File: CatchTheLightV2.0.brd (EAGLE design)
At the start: 45 x 100 mm, 46 parts, among them J1 TC2030-IDC-NL, U1 ATMEGA328PB-ANR

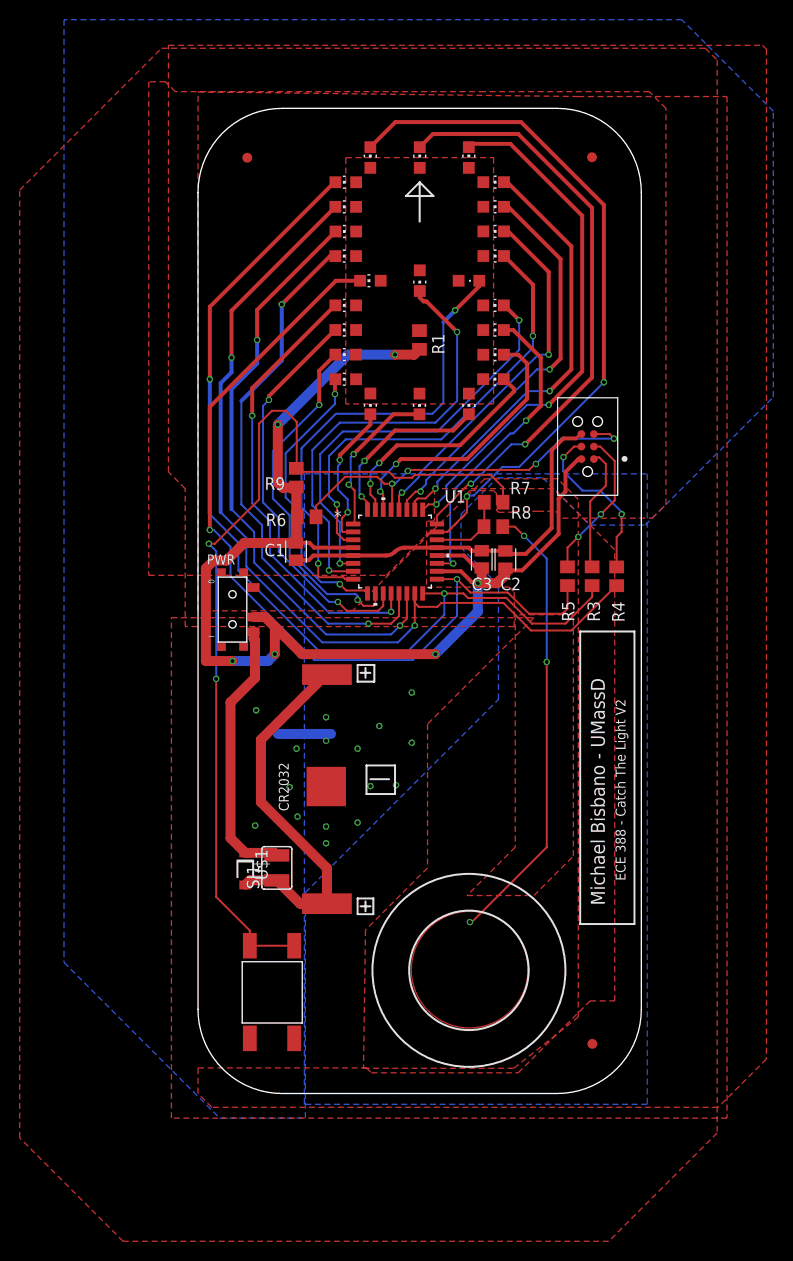
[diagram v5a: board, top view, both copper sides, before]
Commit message: Board Updated to meet some issue requirements
Fiducials relocated according to spec
Silkscreen labels updated

Silkscreen over battery pads removed. Thermal Relief restored on GND pad.
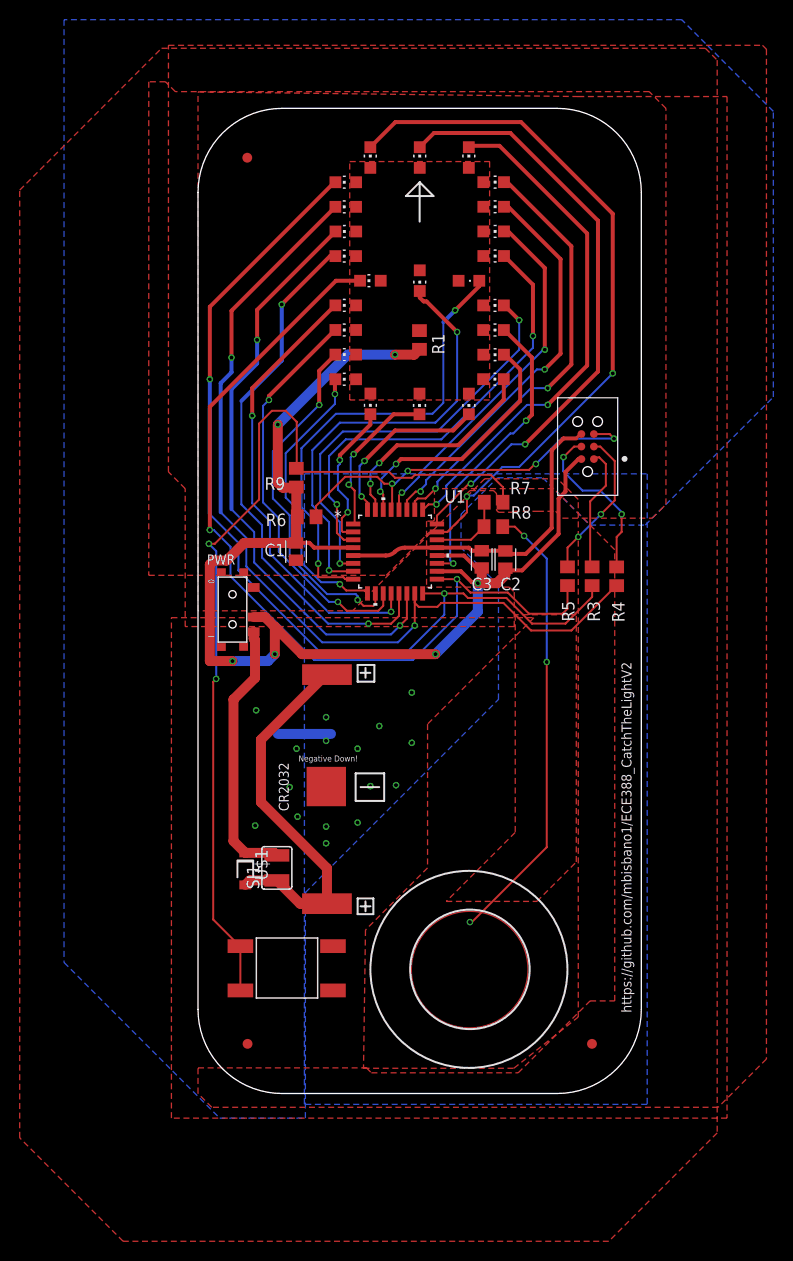
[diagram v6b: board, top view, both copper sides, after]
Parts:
- moved U$5 90.0 mm to (40.0, 5.04)
- moved U$4 35.0 mm to (5.03, 5.04)
- moved PB2 7.49 mm to (3.00, 15.7), turned to 0 degrees
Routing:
- net GND: track 44.7 -> 38.7 mm
- net PD0: track 27.8 -> 26.1 mm
- net PE2: track 31.6 -> 30.3 mm
- net PD1: track 23.7 -> 22.7 mm
- net PC5: track 37.4 -> 36.5 mm
- net PC0: track 70.4 -> 71.2 mm
- net PC2: track 53.2 -> 52.5 mm
- net VCC: track 130.2 -> 129.6 mm
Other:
- board text added: "11/9/2020"
- board text added: "ECE 388 - UMassD"
- board text added: "Michael Bisbano"
- board text added: "Negative Down!"
- board text added: "Rev: B"
- board text added: "https://github.com/mbisbano1/ECE388_CatchTheLightV2"
- board text removed: "ECE 388 - Catch The Light V2"
- board text removed: "Michael Bisbano - UMassD"

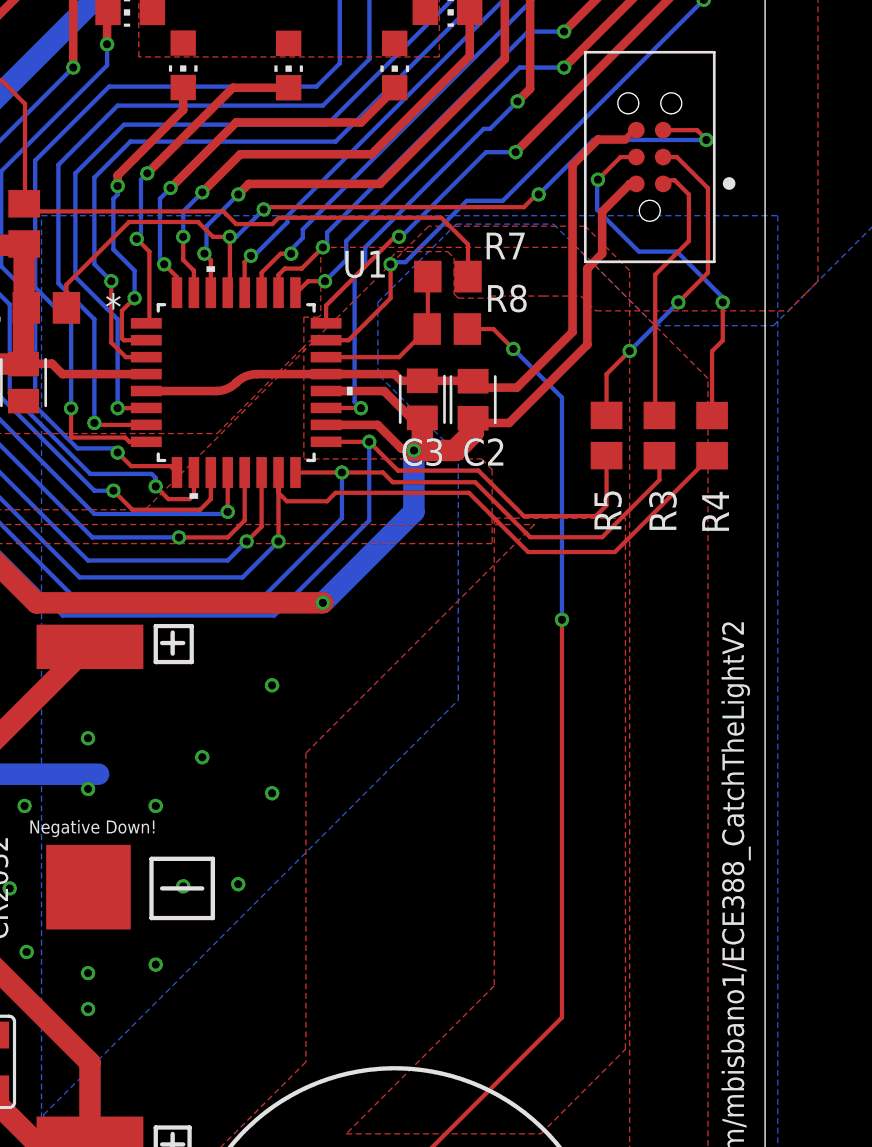
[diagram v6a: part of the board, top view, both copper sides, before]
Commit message: Removed Programming line resistors
Removed programming line resistors and renamed plug of nails to bed of nails.
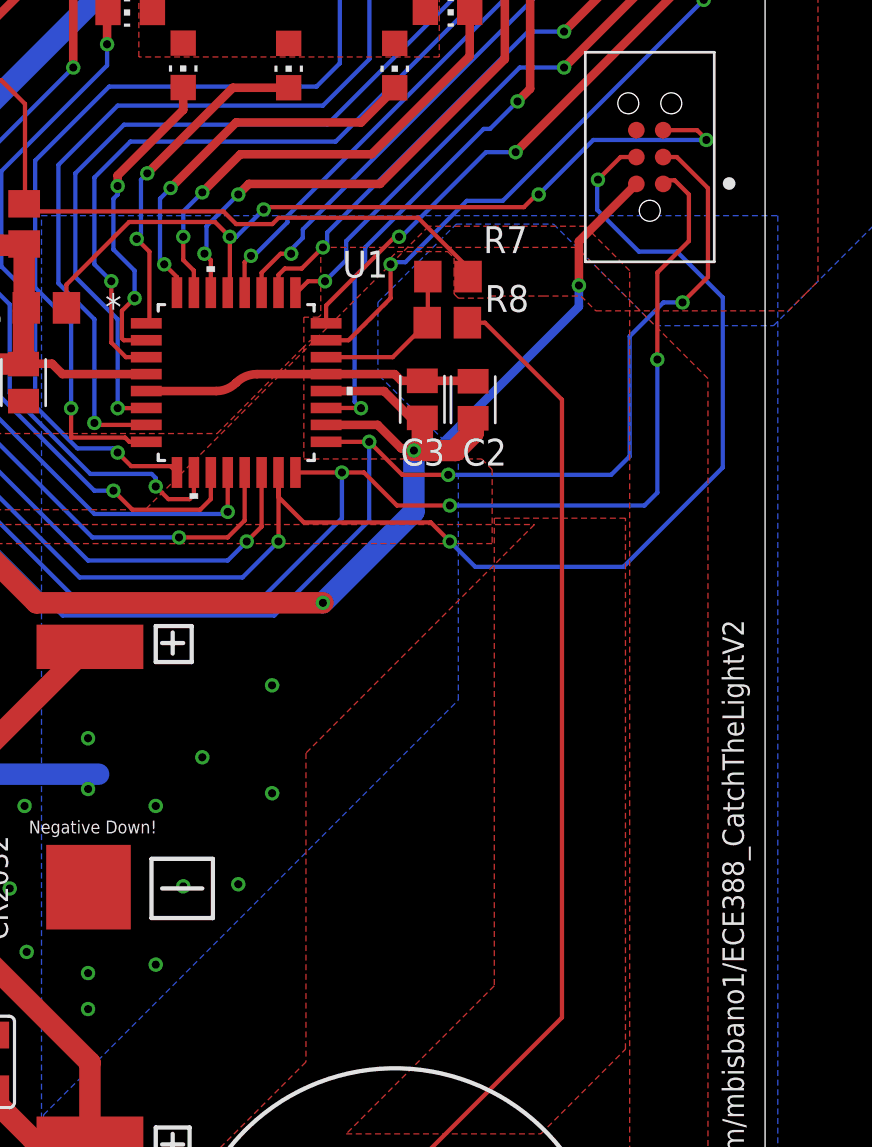
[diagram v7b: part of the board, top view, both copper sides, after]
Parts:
- removed R3, R4, R5: 330, rcl:R0805
- moved R7 0.30 mm to (30.0, 57.8)
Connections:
- removed net MISO: J1.1, R3.2
- removed net MOSI: J1.4, R4.2
- removed net SCK: J1.3, R5.2
- net PB3: now also J1.4; no longer R4.1
- net PB4: now also J1.1; no longer R3.1
- net PB5: now also J1.3; no longer R5.1
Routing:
- net PB3: track 91.5 -> 111.5 mm, vias 2 -> 4
- net GND: track 38.7 -> 21.1 mm
- net MOSI: track 17.1 -> 0.00 mm, vias 2 -> 0
- net PB5: track 88.2 -> 103.8 mm, vias 2 -> 4
- net SCK: track 15.5 -> 0.00 mm, vias 2 -> 0
- net PB4: track 94.7 -> 108.2 mm, vias 2 -> 4
- net MISO: track 12.8 -> 0.00 mm
- net VCC: track 129.6 -> 131.5 mm, vias 6 -> 7
- net SPARE_BUTTON_SIGNAL: track 94.9 -> 94.3 mm
- net QTOUCH: vias 3 -> 1

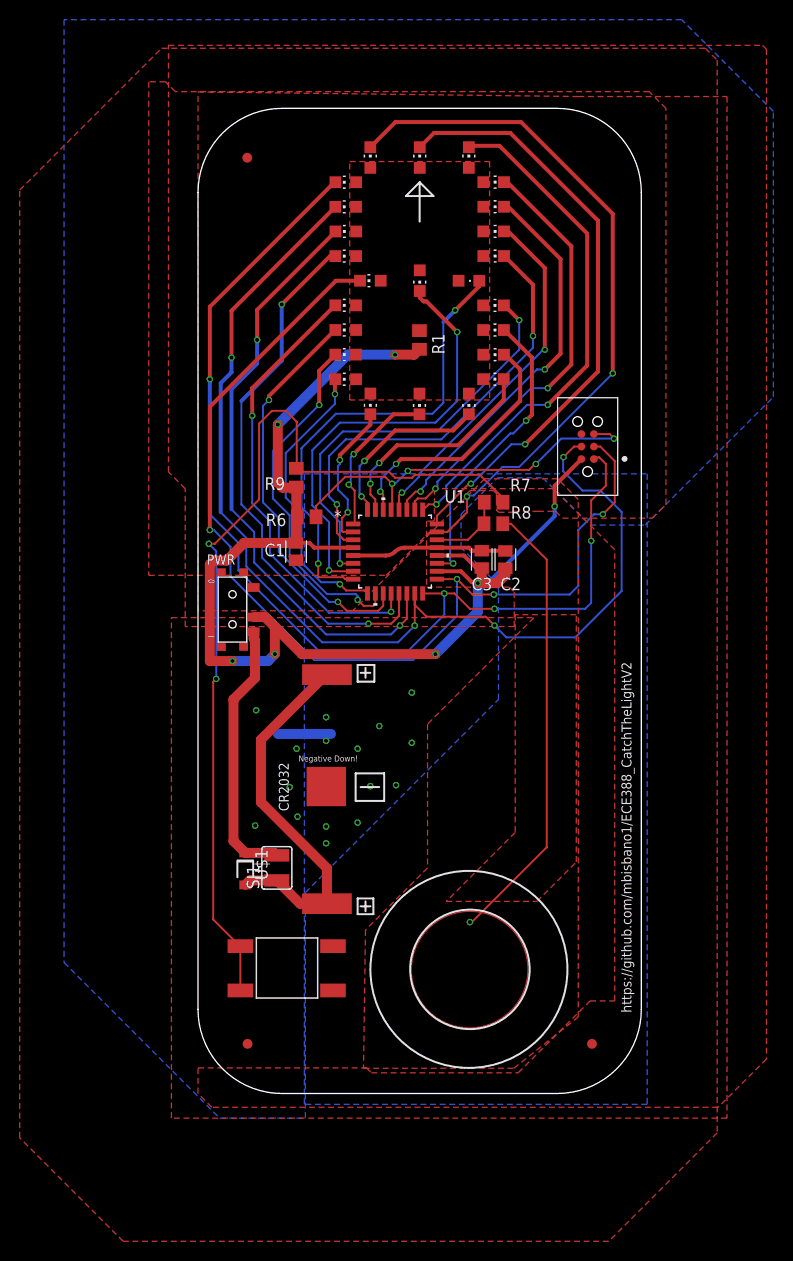
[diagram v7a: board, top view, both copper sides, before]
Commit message: PMOS Reverse Protection in Schematic and Board
Swapped in PMOS over Schottky diode for reverse protection
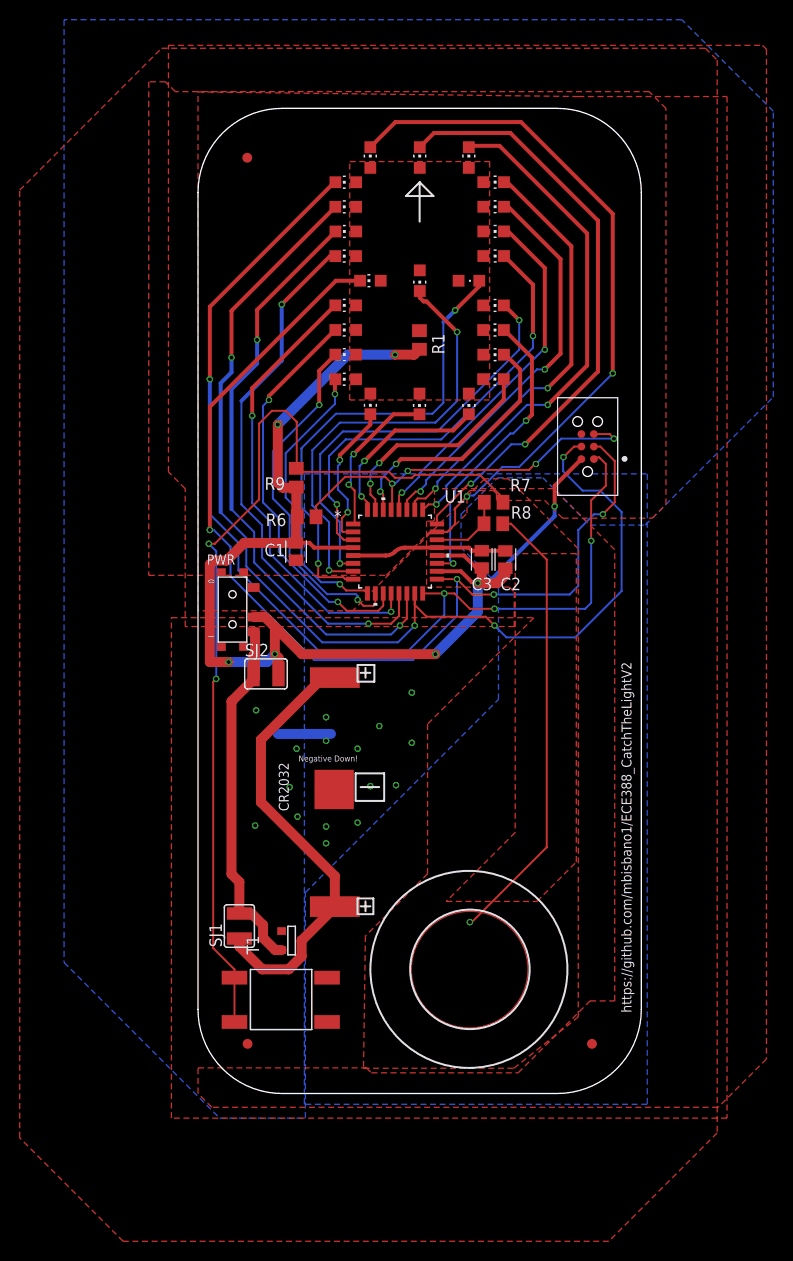
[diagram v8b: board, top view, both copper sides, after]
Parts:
- removed U$1: SCHOTTKY_SS14L, ECE_388_CustomParts_V1.1:SOD123FL
- added SJ2: NOPOP, ECE388:SJW
- added T1: (no value), zetex:SOT-23
- SJ1: value (none) -> NOPOP
- moved SJ1 7.02 mm to (4.20, 17.0)
- moved PB2 3.26 mm to (2.40, 12.5)
- moved BAT1 0.85 mm to (17.4, 20.0)
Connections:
- net GND: now also T1.3
- net PROTECTED_VBAT: now also SJ2.1, T1.2; no longer U$1.C
- net VCC: now also SJ2.2
- net VCC_BATTERY: now also T1.1; no longer U$1.A
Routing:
- net PROTECTED_VBAT: track 27.2 -> 39.0 mm
- net VCC_BATTERY: track 38.3 -> 45.6 mm
- net SPARE_BUTTON_SIGNAL: track 94.3 -> 97.2 mm
- net VCC: track 131.5 -> 133.8 mm
